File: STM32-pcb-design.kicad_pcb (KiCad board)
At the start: 2 copper layers, 35 x 30 mm, 35 parts, among them J1 USB_B_Micro, J2 Conn_01x04_Pin, J3 Conn_01x04_Pin, J4 Conn_01x04_Pin, SW1 SW_SPDT, SW2 SW_SPDT, SW3 SW_SPDT, U1 STM32F103C8Tx, U2 AMS1117-3.3, Y1 16MHz

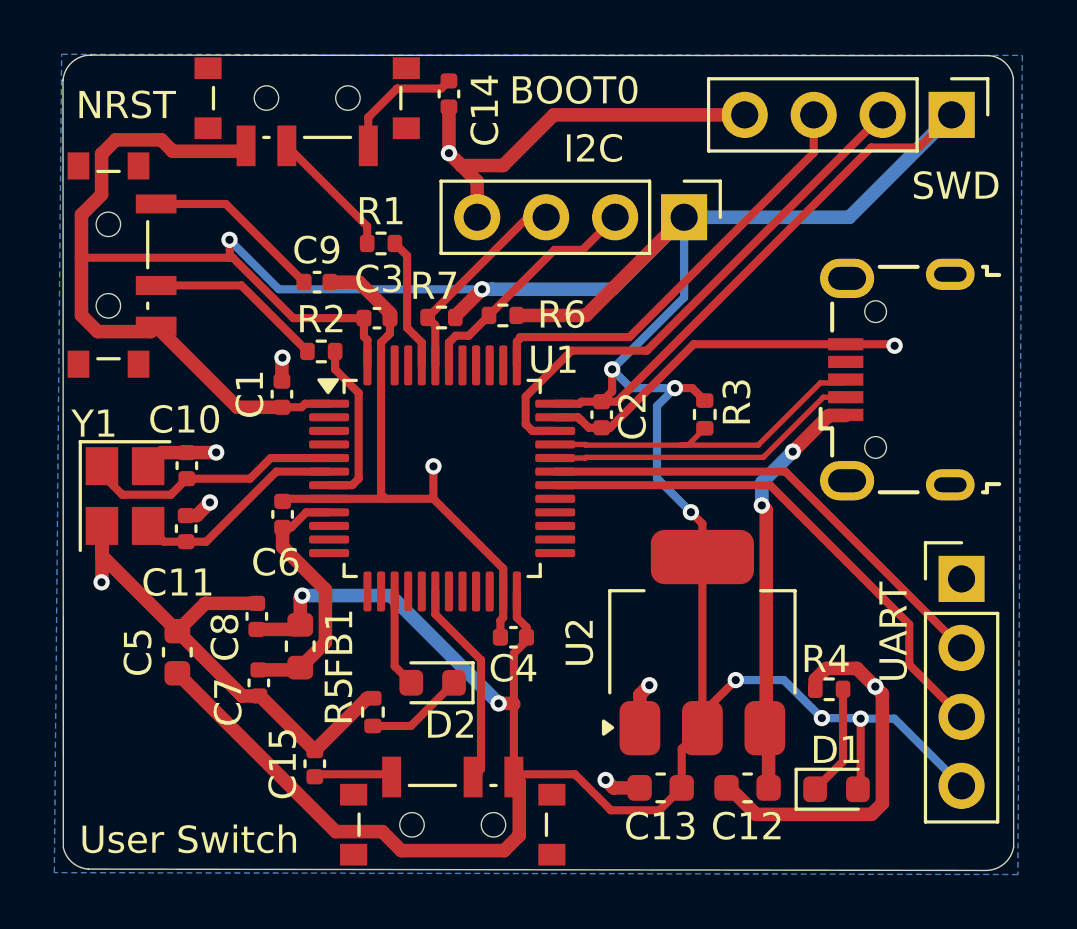
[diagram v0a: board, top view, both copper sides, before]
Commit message: Changed the routing for the usb connector
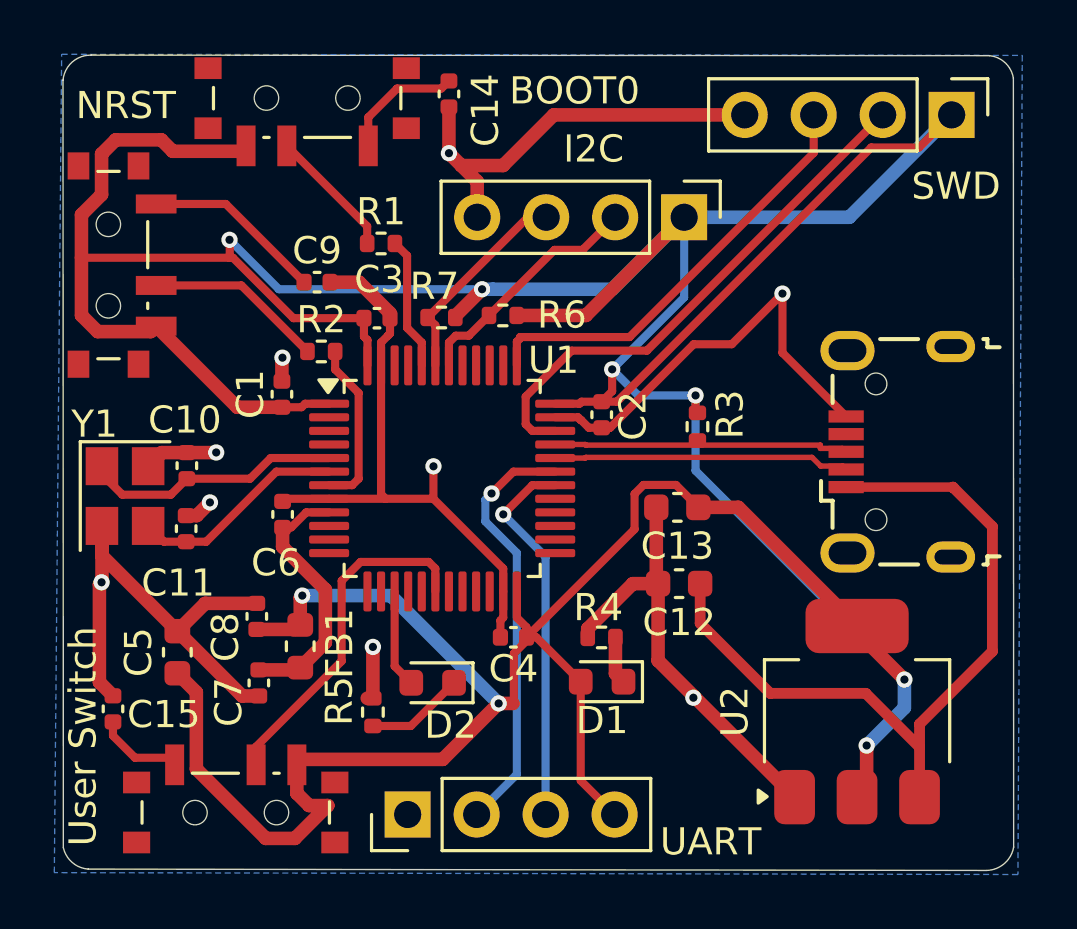
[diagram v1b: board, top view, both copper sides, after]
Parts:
- moved J4 22.2 mm to (103.3, 58.5), turned to 90 degrees
- moved C13 10.3 mm to (113.2, 47.2)
- moved D1 9.50 mm to (110.4, 53.7), turned to 180 degrees
- moved R4 8.59 mm to (110.4, 52.0)
- moved SW3 8.00 mm to (97.0, 58.1)
- moved C12 7.93 mm to (113.3, 50.0)
- moved C15 7.70 mm to (92.4, 54.7)
- moved U2 6.24 mm to (119.8, 54.8)
- moved J1 2.66 mm to (121.3, 45.2)
- moved R3 0.52 mm to (114.0, 44.3)
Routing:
- net VBUS: track 15.5 -> 28.5 mm, vias 2 -> 0
- net +3.3V: track 182.1 -> 191.9 mm, vias 10 -> 8
- net /USART1_TX: track 19.4 -> 14.1 mm, vias 0 -> 1
- net Net-(SW3-B): track 7.65 -> 12.8 mm
- net GND: track 94.1 -> 96.6 mm, vias 10 -> 9
- net Net-(D1-K): track 4.11 -> 1.75 mm
- net /USART1_RX: track 17.7 -> 15.7 mm, vias 0 -> 1
- net /USB_D+: track 12.8 -> 10.9 mm
- net /USB_D-: track 11.6 -> 10.9 mm

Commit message: Re-oriented the AMS1117
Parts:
- moved C13 11.2 mm to (123.2, 52.2), turned to 90 degrees
- moved C12 4.95 mm to (114.2, 54.9), turned to -90 degrees
- moved U2 1.15 mm to (118.7, 54.9), turned to -90 degrees
- moved R3 1.06 mm to (115.0, 44.3)
- moved J1 0.12 mm to (121.3, 45.1)
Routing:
- net VBUS: track 28.5 -> 10.8 mm
- net +3.3V: track 191.9 -> 182.0 mm, vias 8 -> 7
- net GND: track 96.6 -> 95.3 mm, vias 9 -> 10

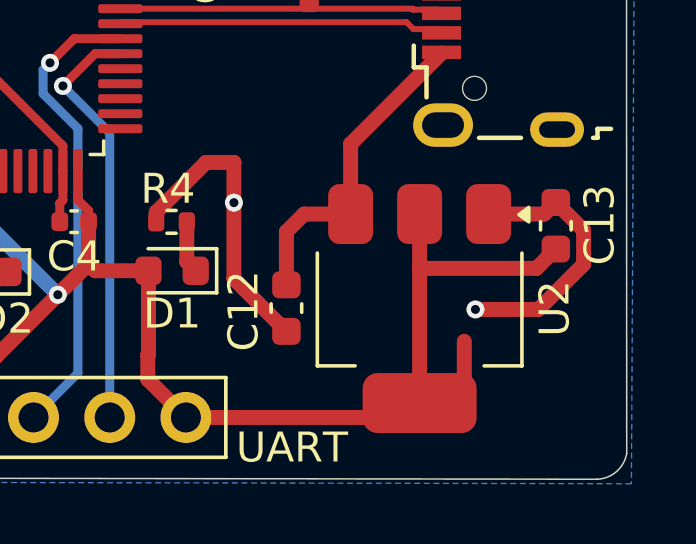
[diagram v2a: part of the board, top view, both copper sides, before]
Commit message: Moved the ams1117 to avoid soldering issues
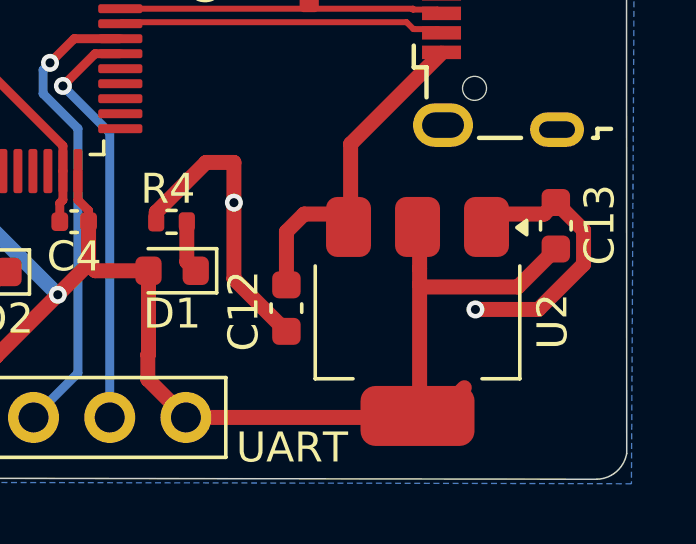
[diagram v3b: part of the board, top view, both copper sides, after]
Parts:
- moved U2 0.44 mm to (118.6, 55.4)
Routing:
- net +3.3V: track 182.0 -> 180.7 mm
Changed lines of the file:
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@@
 	(footprint "Package_TO_SOT_SMD:SOT-223-3_TabPin2"
 		(layer "F.Cu")
-		(at 118.69 54.92 -90)
+		(at 118.62 55.35 -90)
 		(descr "module CMS SOT223 4 pins")
 		(tags "CMS SOT")
@@
 		)
 		(fp_text user "${REFERENCE}"
-			(at 0 0 360)
+			(at 0 0 0)
 			(layer "F.Fab")
 			(effects
@@
 	)
 	(segment
+		(start 121.965 54.2)
+		(end 118.78 54.2)
+		(width 0.5)
+		(layer "F.Cu")
+		(net 2)
+	)
+	(segment
 		(start 99.65 58.22)
 		(end 100.34 58.22)
@@
 	)
 	(segment
-		(start 120.18 56.01)
-		(end 120.18 57.5575)
-		(width 0.5)
-		(layer "F.Cu")
-		(net 2)
-	)
-	(segment
 		(start 94.8 53.35)
 		(end 95.5 54.05)
@@
 	)
 	(segment
+		(start 118.69 53.58)
+		(end 118.69 54.11)
+		(width 0.5)
+		(layer "F.Cu")
+		(net 2)
+	)
+	(segment
 		(start 109.845 40.175)
 		(end 113.46 36.56)
@@
 	)
 	(segment
+		(start 123.23 52.935)
+		(end 121.965 54.2)
+		(width 0.5)
+		(layer "F.Cu")
+		(net 2)
+	)
+	(segment
 		(start 99.375 43.555)
 		(end 98.65 43.555)
@@
 	)
 	(segment
+		(start 118.69 54.11)
+		(end 118.69 58.07)
+		(width 0.5)
+		(layer "F.Cu")
+		(net 2)
+	)
+	(segment
 		(start 122.11 33.99)
 		(end 123.31 32.79)
@@
 	)
 	(segment
-		(start 123.23 52.935)
-		(end 122.585 53.58)
-		(width 0.5)
-		(layer "F.Cu")
-		(net 2)
-	)
-	(segment
 		(start 107.88 53.66)
 		(end 107.655 53.435)
@@
 	)
 	(segment
-		(start 118.69 53.58)
-		(end 118.69 58.07)
-		(width 0.5)
-		(layer "F.Cu")
-		(net 2)
-	)
-	(segment
 		(start 109.68 43.35)
 		(end 110.425 43.35)
@@
 	)
 	(segment
+		(start 118.78 54.2)
+		(end 118.69 54.11)
+		(width 0.5)
+		(layer "F.Cu")
+		(net 2)
+	)
+	(segment
 		(start 97.13 34.13)
 		(end 94.63 34.13)
@@
 		(width 0.5)
 		(layer "F.Cu")
-		(net 2)
-	)
-	(segment
-		(start 122.585 53.58)
-		(end 118.69 53.58)
-		(width 0.5)
-		(layer "F.Cu")

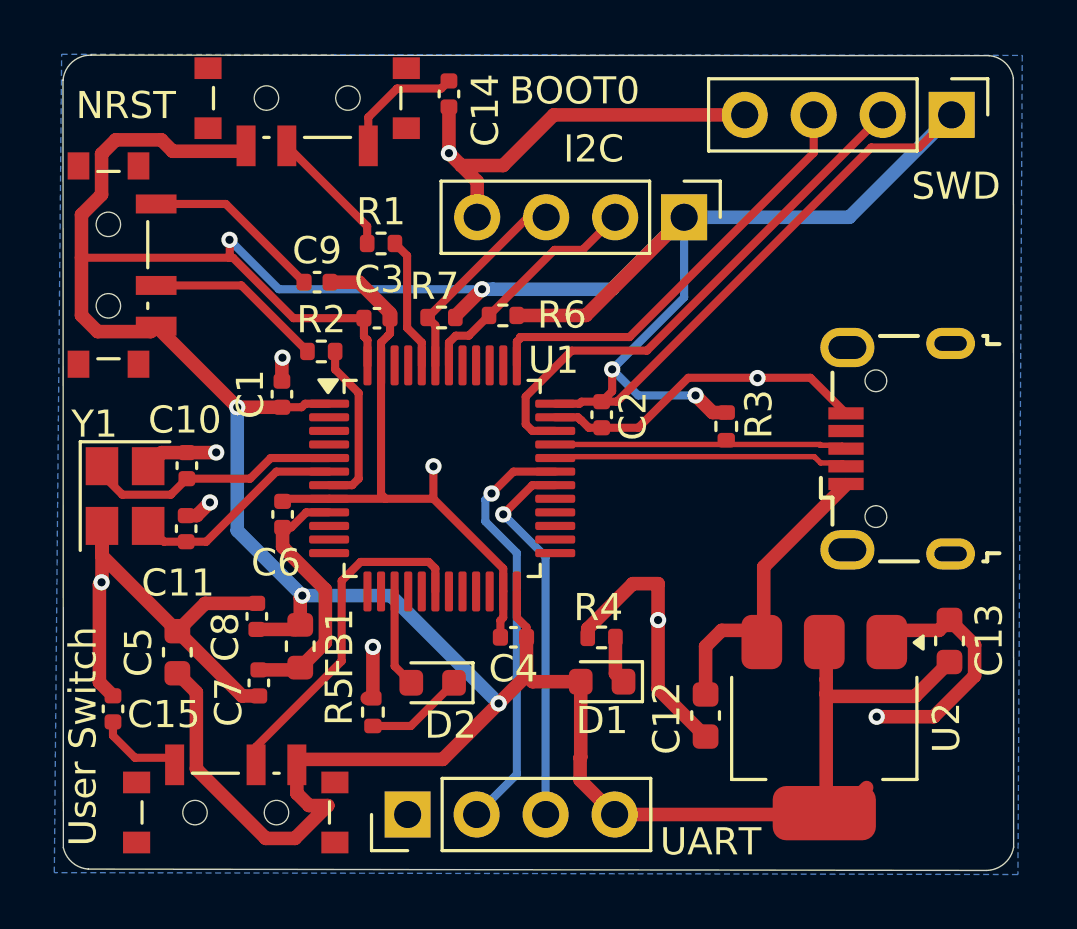
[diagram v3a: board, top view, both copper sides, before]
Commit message: Changed Pull-up to vbus from 3.3V
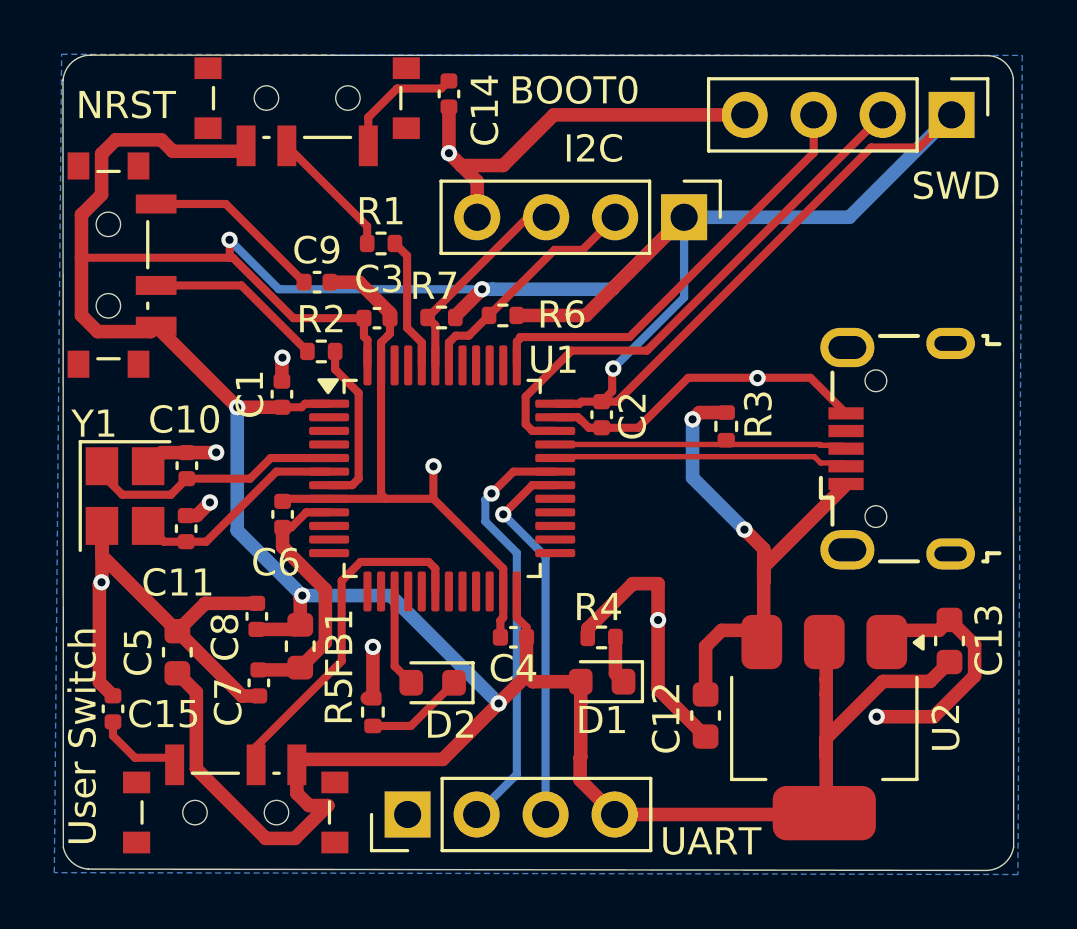
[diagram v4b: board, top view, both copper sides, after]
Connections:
- R3 pad 1: +3.3V -> VBUS
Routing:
- net VBUS: track 10.8 -> 19.2 mm, vias 0 -> 2
- net +3.3V: track 180.7 -> 176.6 mm, vias 7 -> 6
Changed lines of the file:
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@@
 			(layers "F.Cu" "F.Paste" "F.Mask")
 			(roundrect_rratio 0.25)
-			(net 2 "+3.3V")
+			(net 7 "VBUS")
 			(pintype "passive")
 		)
@@
 	)
 	(segment
-		(start 121.965 54.2)
-		(end 118.78 54.2)
-		(width 0.5)
-		(layer "F.Cu")
-		(net 2)
-	)
-	(segment
 		(start 99.65 58.22)
 		(end 100.34 58.22)
@@
 	)
 	(segment
+		(start 122.515 53.65)
+		(end 120.78 53.65)
+		(width 0.5)
+		(layer "F.Cu")
+		(net 2)
+	)
+	(segment
 		(start 101.67 40.275)
 		(end 99.072106 40.275)
@@
 	)
 	(segment
-		(start 120.18 57.5575)
-		(end 119.8275 57.91)
-		(width 0.5)
-		(layer "F.Cu")
-		(net 2)
-	)
-	(segment
 		(start 118.69 53.58)
 		(end 118.69 54.11)
@@
 	)
 	(segment
-		(start 114.51 43.75)
-		(end 113.88 43.12)
-		(width 0.5)
-		(layer "F.Cu")
-		(net 2)
-	)
-	(segment
 		(start 98.056497 59.43)
 		(end 99.13 59.43)
@@
 	)
 	(segment
+		(start 118.69 54.11)
+		(end 118.69 56.4)
+		(width 0.5)
+		(layer "F.Cu")
+		(net 2)
+	)
+	(segment
 		(start 109.6525 53.66)
 		(end 107.88 53.66)
@@
 	)
 	(segment
-		(start 123.23 52.935)
-		(end 121.965 54.2)
-		(width 0.5)
-		(layer "F.Cu")
-		(net 2)
-	)
-	(segment
 		(start 99.375 43.555)
 		(end 98.65 43.555)
@@
 	)
 	(segment
-		(start 118.69 54.11)
-		(end 118.69 58.07)
-		(width 0.5)
-		(layer "F.Cu")
-		(net 2)
-	)
-	(segment
 		(start 122.11 33.99)
 		(end 123.31 32.79)
@@
 	)
 	(segment
-		(start 115.01 43.75)
-		(end 114.51 43.75)
-		(width 0.5)
-		(layer "F.Cu")
-		(net 2)
-	)
-	(segment
 		(start 110.81 42.16)
 		(end 110.81 42.965)
@@
 	)
 	(segment
+		(start 118.69 55.74)
+		(end 118.69 56.4)
+		(width 0.5)
+		(layer "F.Cu")
+		(net 2)
+	)
+	(segment
 		(start 100.3875 43.425)
 		(end 99.505 43.425)
@@
 	)
 	(segment
+		(start 118.69 56.4)
+		(end 118.69 58.07)
+		(width 0.5)
+		(layer "F.Cu")
+		(net 2)
+	)
+	(segment
 		(start 101.8 42.0125)
 		(end 101.8 41.08)
@@
 	)
 	(segment
+		(start 120.78 53.65)
+		(end 118.69 55.74)
+		(width 0.5)
+		(layer "F.Cu")
+		(net 2)
+	)
+	(segment
 		(start 97.005 43.555)
 		(end 98.65 43.555)
@@
 	)
 	(segment
-		(start 118.78 54.2)
-		(end 118.69 54.11)
-		(width 0.5)
-		(layer "F.Cu")
-		(net 2)
-	)
-	(segment
 		(start 97.13 34.13)
 		(end 94.63 34.13)
@@
 	)
 	(segment
+		(start 123.23 52.935)
+		(end 122.515 53.65)
+		(width 0.5)
+		(layer "F.Cu")
+		(net 2)
+	)
+	(segment
 		(start 109.63 57.28)
 		(end 109.63 56.46)
@@
 		(width 0.5)
 		(layer "F.Cu")
-		(net 2)
-	)
-	(via
-		(at 113.88 43.12)
-		(size 0.6)
-		(drill 0.3)
-		(layers "F.Cu" "B.Cu")
 		(net 2)
 	)
@@
 	)
 	(via
-		(at 110.81 42.16)
+		(at 110.85 42.13)
 		(size 0.6)
 		(drill 0.3)
@@
 	(segment
 		(start 110.81 42.16)
+		(end 110.84 42.13)
+		(width 0.3)
+		(layer "B.Cu")
+		(net 2)
+	)
+	(segment
+		(start 110.84 42.13)
+		(end 110.85 42.13)
+		(width 0.3)
+		(layer "B.Cu")
+		(net 2)
+	)
+	(segment
+		(start 110.85 42.12)
 		(end 113.46 39.51)
 		(width 0.3)
@@
 	)
 	(segment
-		(start 110.81 42.16)
-		(end 111.77 43.12)
-		(width 0.3)
-		(layer "B.Cu")
-		(net 2)
-	)
-	(segment
 		(start 106.41 39.21)
 		(end 110.81 39.21)
@@
 	)
 	(segment
-		(start 111.77 43.12)
-		(end 113.88 43.12)
-		(width 0.3)
-		(layer "B.Cu")
-		(net 2)
-	)
-	(segment
 		(start 99.4 50.49)
 		(end 97.005 48.095)
@@
 	)
 	(segment
+		(start 110.85 42.13)
+		(end 110.85 42.12)
+		(width 0.3)
+		(layer "B.Cu")
+		(net 2)
+	)
+	(segment
 		(start 99.2425 53.225)
 		(end 99.325 53.1425)
@@
 	)
 	(segment
+		(start 115.68 48.06)
+		(end 116.39 48.77)
+		(width 0.5)
+		(layer "F.Cu")
+		(net 7)
+	)
+	(segment
+		(start 116.39 51.77)
+		(end 116.39 49.99)
+		(width 0.5)
+		(layer "F.Cu")
+		(net 7)
+	)
+	(segment
+		(start 115.01 43.75)
+		(end 114.02 43.75)
+		(width 0.5)
+		(layer "F.Cu")
+		(net 7)
+	)
+	(segment
+		(start 116.39 48.77)
+		(end 116.39 49.99)
+		(width 0.5)
+		(layer "F.Cu")
+		(net 7)
+	)
+	(segment
 		(start 116.39 49.435)
 		(end 119.42 46.405)
@@
 	)
 	(segment
+		(start 116.39 49.99)
+		(end 116.39 49.435)
+		(width 0.5)
+		(layer "F.Cu")
+		(net 7)
+	)
+	(segment
 		(start 114.25 52.36)
 		(end 114.84 51.77)
@@
 	)
 	(segment
-		(start 116.39 51.77)
-		(end 116.39 49.435)
+		(start 114.02 43.75)
+		(end 113.77 44)
 		(width 0.5)
 		(layer "F.Cu")
 		(net 7)
 	)
+	(via
+		(at 115.68 48.06)
+		(size 0.6)
+		(drill 0.3)
+		(layers "F.Cu" "B.Cu")
+		(net 7)
+	)
+	(via
+		(at 113.77 44)
+		(size 0.6)
+		(drill 0.3)
+		(layers "F.Cu" "B.Cu")
+		(net 7)
+	)
+	(segment
+		(start 113.77 44)
+		(end 113.77 46.15)
+		(width 0.5)
+		(layer "B.Cu")
+		(net 7)
+	)
+	(segment
+		(start 113.77 46.15)
+		(end 115.68 48.06)
+		(width 0.5)
+		(layer "B.Cu")
+		(net 7)
+	)
